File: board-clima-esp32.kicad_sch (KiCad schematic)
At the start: 32 parts, among them IC1 ESP32-S3-WROOM-1-N4, J1 Conn_01x02_Pin, J2 Screw_Terminal_01x03, J3 Conn_01x04_Pin, J4 Conn_01x04_Pin, J5 Conn_01x04_Pin, J6 USB_C_Receptacle, Q1 AO3400A, SW1 RESET, SW2 BOOT, U1 AMS1117-3.3, U2 JZC-32F/C

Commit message: cleanup and some helper in schematic
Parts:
- J4: footprint Connector_PinHeader_1.00mm:PinHeader_1x05_P1.00mm_Vertical -> Connector_PinHeader_2.54mm:PinHeader_1x05_P2.54mm_Vertical
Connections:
- net GND: no longer J6.S1 (SHIELD)
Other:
- note added: "I2C Bus Address: 0x77"
- moved on the sheet: C1, C2, C3, C4, D3, F1, J6, R1, R2, R4, R5, R6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

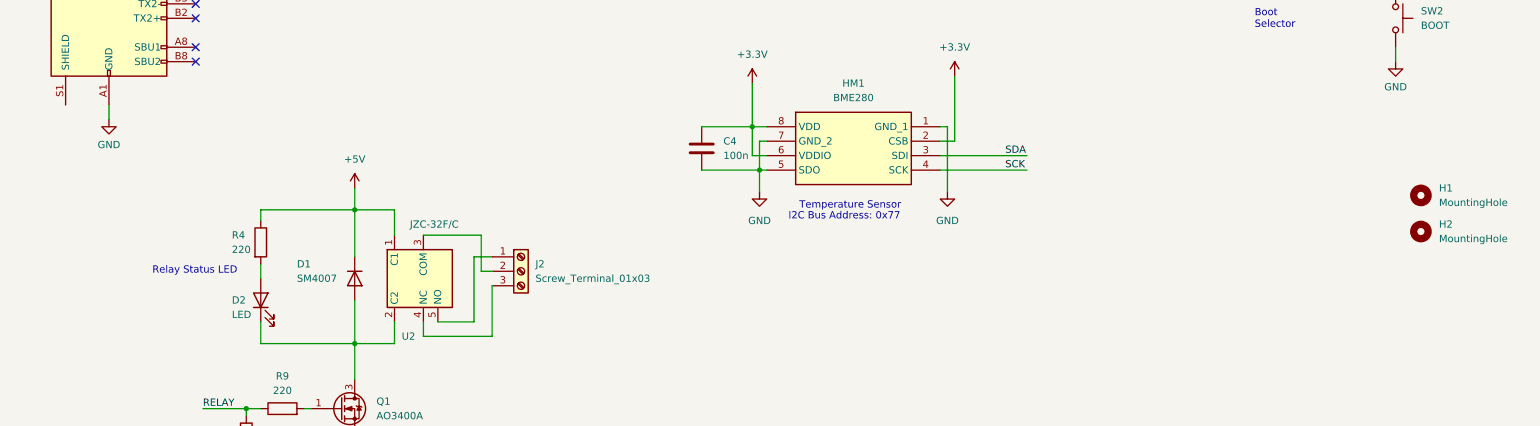
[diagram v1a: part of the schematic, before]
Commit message: added bypass jumper
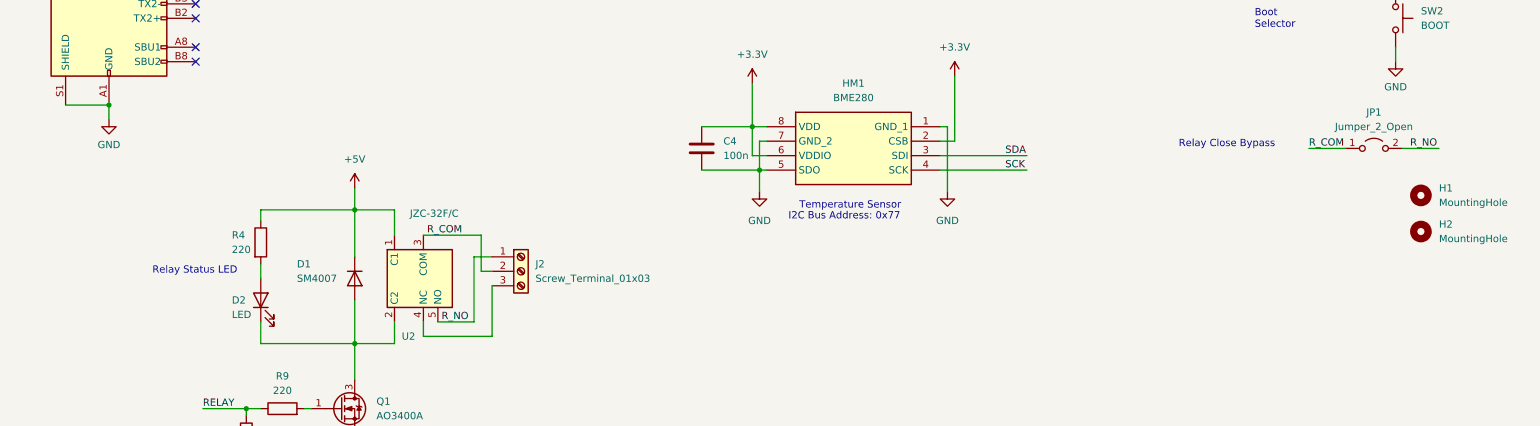
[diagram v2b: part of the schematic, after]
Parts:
- added JP1: Jumper_2_Open, TestPoint:TestPoint_2Pads_Pitch2.54mm_Drill0.8mm, symbol Jumper:Jumper_2_Open
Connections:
- net GND: now also J6.S1 (SHIELD)
- net R_NO: now reaches J2.1 (Pin_1), U2.5 (NO)
- net R_NO: now also JP1.2 (B)
- net R_COM: now reaches J2.2 (Pin_2), U2.3 (COM)
- net R_COM: now also JP1.1 (A)
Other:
- note added: "Relay Close Bypass"
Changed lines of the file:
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@@
     (company "Edoardo Fullin")
+  )
+  (junction (at 30.48 121.92) (diameter 0) (color 0 0 0 0)
   )
   (junction (at 143.51 125.73) (diameter 0) (color 0 0 0 0)
@@
     (stroke (width 0) (type default))
   )
+  (wire (pts (xy 257.81 129.54) (xy 264.16 129.54))
+    (stroke (width 0) (type default))
+  )
   (wire (pts (xy 110.49 74.93) (xy 120.65 74.93))
     (stroke (width 0) (type default))
@@
     (stroke (width 0) (type default))
   )
+  (wire (pts (xy 241.3 129.54) (xy 247.65 129.54))
+    (stroke (width 0) (type default))
+  )
   (wire (pts (xy 97.79 162.56) (xy 85.725 162.56))
     (stroke (width 0) (type default))
   )
   (wire (pts (xy 176.53 82.55) (xy 176.53 85.09))
+    (stroke (width 0) (type default))
+  )
+  (wire (pts (xy 22.86 121.92) (xy 30.48 121.92))
     (stroke (width 0) (type default))
   )
@@
     (effects (font (size 1.27 1.27)) (justify left bottom))
   )
+  (text "Relay Close Bypass" (at 218.44 129.54 0)
+    (effects (font (size 1.27 1.27)) (justify left bottom))
+  )
   (text "Additional\nGPIO" (at 228.6 90.17 0)
     (effects (font (size 1.27 1.27)) (justify left bottom))
@@
     (effects (font (size 1.27 1.27)) (justify left bottom))
   )
+  (label "R_COM" (at 241.3 129.54 0) (fields_autoplaced)
+    (effects (font (size 1.27 1.27)) (justify left bottom))
+  )
+  (label "R_NO" (at 88.9 160.02 0) (fields_autoplaced)
+    (effects (font (size 1.27 1.27)) (justify left bottom))
+  )
   (label "UART_TX" (at 241.3 40.64 0) (fields_autoplaced)
     (effects (font (size 1.27 1.27)) (justify left bottom))
@@
     (effects (font (size 1.27 1.27)) (justify left bottom))
   )
+  (label "R_NO" (at 259.08 129.54 0) (fields_autoplaced)
+    (effects (font (size 1.27 1.27)) (justify left bottom))
+  )
   (label "SDA" (at 241.3 20.32 0) (fields_autoplaced)
     (effects (font (size 1.27 1.27)) (justify left bottom))
@@
   )
   (label "BOOT" (at 182.88 31.75 0) (fields_autoplaced)
+    (effects (font (size 1.27 1.27)) (justify left bottom))
+  )
+  (label "R_COM" (at 86.36 144.78 0) (fields_autoplaced)
     (effects (font (size 1.27 1.27)) (justify left bottom))
   )
@@
         (path "/ec184202-d4fa-4f1f-9fe7-c32d14dd4c20"
           (reference "#PWR07") (unit 1)
+        )
+      )
+    )
+  )
+  (symbol (lib_id "Jumper:Jumper_2_Open") (at 252.73 129.54 0) (unit 1)
+    (in_bom yes) (on_board yes) (dnp no) (fields_autoplaced)
+    (property "Reference" "JP1" (at 252.73 123.19 0)
+      (effects (font (size 1.27 1.27)))
+    )
+    (property "Value" "Jumper_2_Open" (at 252.73 125.73 0)
+      (effects (font (size 1.27 1.27)))
+    )
+    (property "Footprint" "TestPoint:TestPoint_2Pads_Pitch2.54mm_Drill0.8mm" (at 252.73 129.54 0)
+      (effects (font (size 1.27 1.27)) hide)
+    )
+    (property "Datasheet" "~" (at 252.73 129.54 0)
+      (effects (font (size 1.27 1.27)) hide)
+    )
+    (pin "1")
+    (pin "2")
+    (instances
+      (project "board-clima-esp32"
+        (path "/ec184202-d4fa-4f1f-9fe7-c32d14dd4c20"
+          (reference "JP1") (unit 1)
         )
       )
@@
       (effects (font (size 1.27 1.27)) (justify left))
     )
-    (property "Value" "JZC-32F/C" (at 87.63 142.875 0)
-      (effects (font (size 1.27 1.27)))
-    )
+    (property "Value" "JZC-32F/C" (at 87.63 140.97 0)
+      (effects (font (size 1.27 1.27)))
+    )

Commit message: refactor schematic
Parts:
- added R10: 0, symbol Device:R
- J1: symbol Connector:Conn_01x03_Pin -> Connector:Conn_01x04_Pin
- R4, R5: value 220 -> 1k
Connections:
- net +3.3V: now also J1.4 (Pin_4)
- net +5V: now also R10.1; no longer U2.1 (C1)
- net R_NC: now reaches J2.3 (Pin_3), U2.4 (NC)
- new net: R10.2, U2.1 (C1)
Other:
- note added: "Actuators Connections"
- note added: "ESP32S3"
- note added: "External I/O"
- note added: "I2C"
- note added: "JTAG / IO"
- note added: "Junk"
- note added: "Onboard Relay"
- note added: "Onboard Temperature Sensor BME280"
- note added: "Relay ON"
- note added: "Relay Terminals"
- note added: "Relay current limit resistor"
- note added: "USB"
- note removed: "Additional I2C"
- note removed: "JTAG"
- note removed: "Relay Status LED"
- moved on the sheet: C1, C2, C3, C4, D1, D2, D3, F1, H1, H2, HM1, IC1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

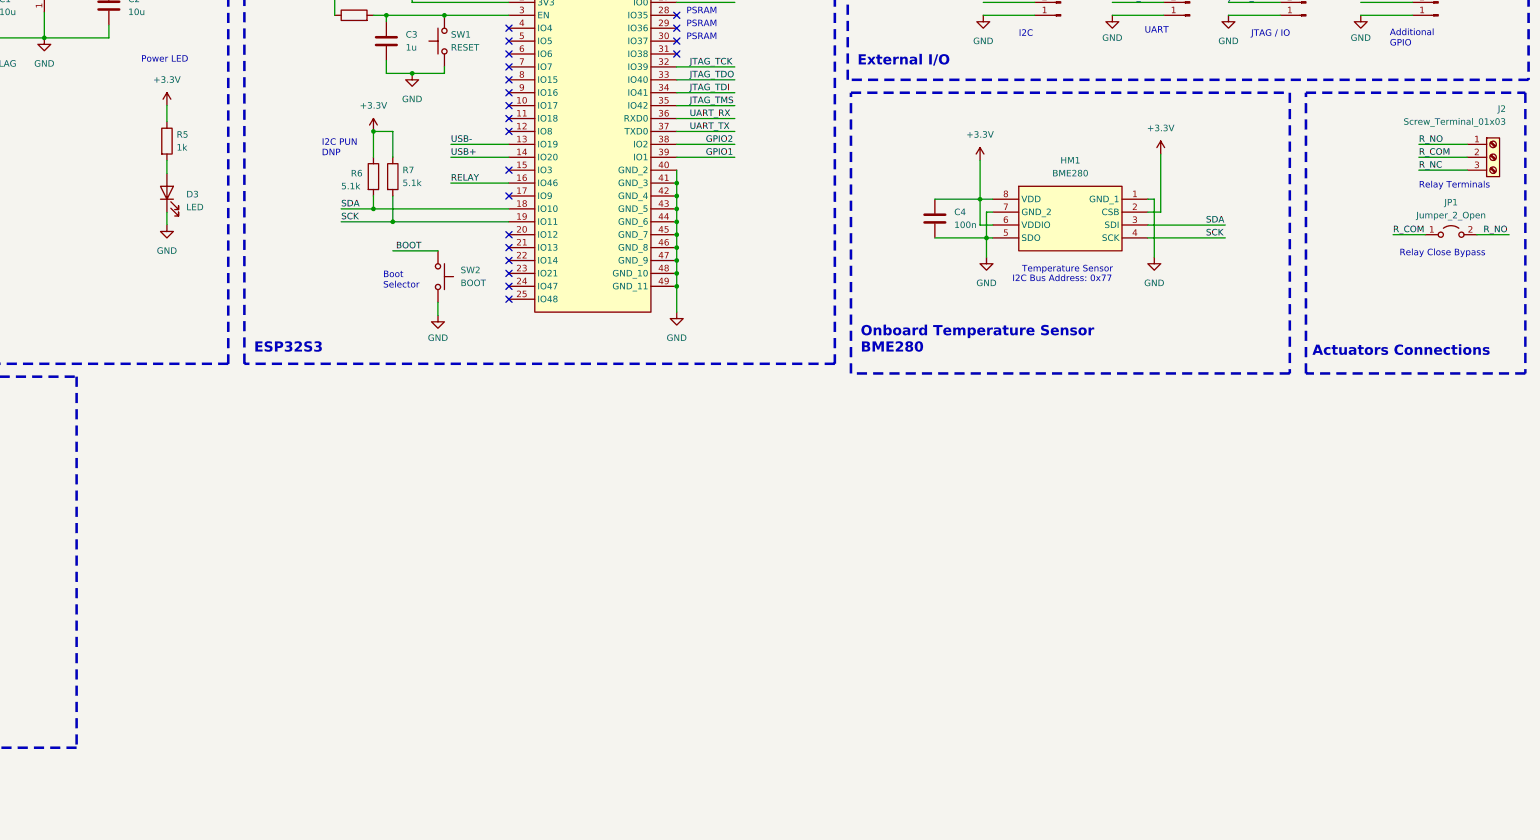
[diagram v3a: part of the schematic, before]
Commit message: OT schematic, relay spice
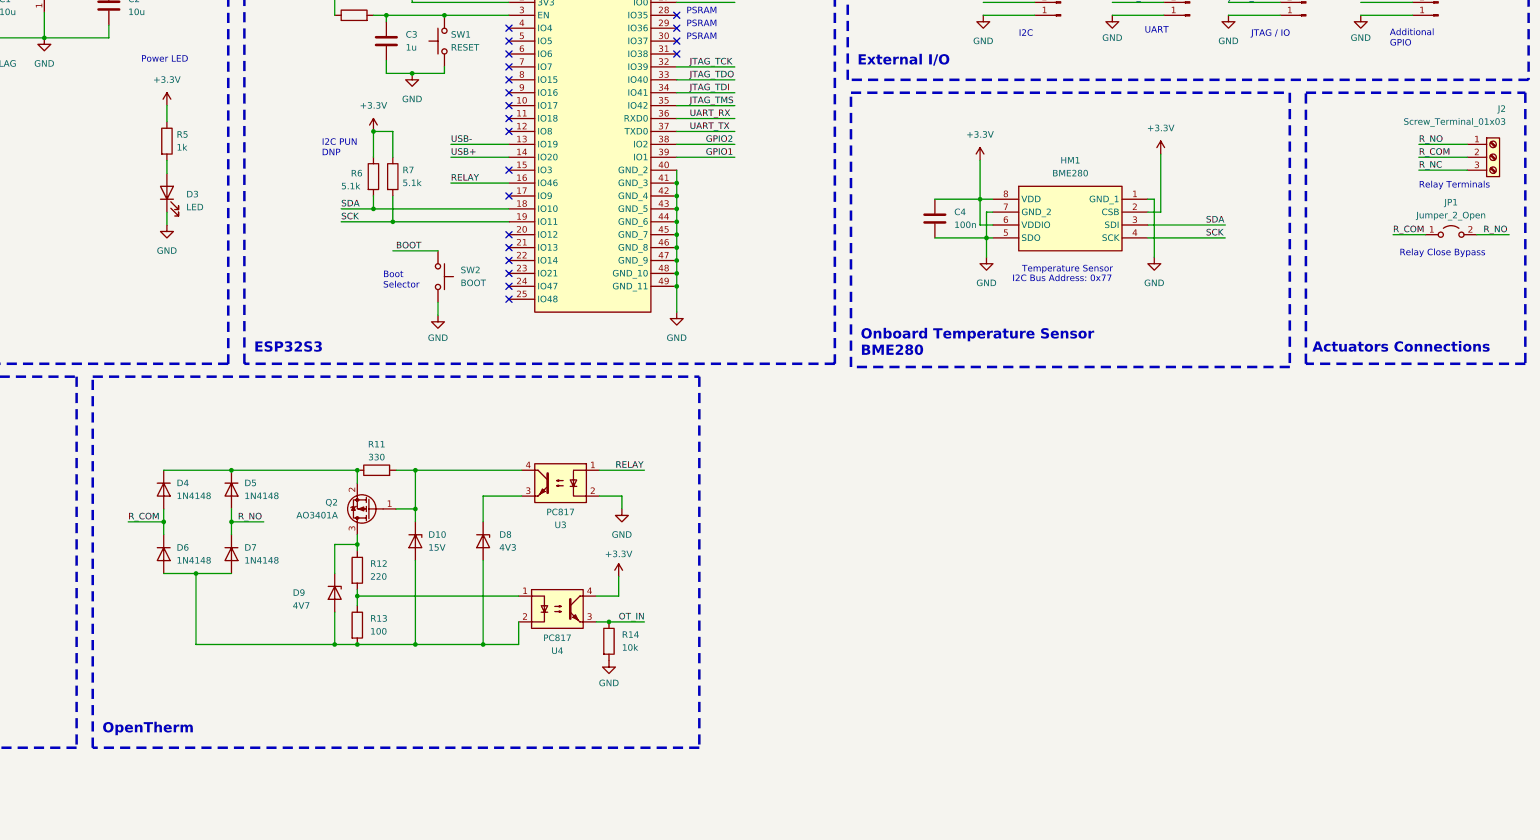
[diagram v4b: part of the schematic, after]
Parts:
- added D10: 15V, symbol Device:D_Zener
- added D4, D5, D6, D7: 1N4148, Diode_THT:D_DO-35_SOD27_P7.62mm_Horizontal, symbol Diode:1N4148
- added D8: 4V3, symbol Device:D_Zener
- added D9: 4V7, symbol Device:D_Zener
- added Q2: AO3401A, Package_TO_SOT_SMD:SOT-23, symbol Transistor_FET:AO3401A
- added R11: 330, symbol Device:R
- added R12: 220, symbol Device:R
- added R13: 100, symbol Device:R
- added R14: 10k, symbol Device:R
- added U3, U4: PC817, Package_DIP:DIP-4_W7.62mm, symbol Isolator:PC817
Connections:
- net +3.3V: now also U4.4
- net GND: now also R14.2, U3.2
- net RELAY: now also U3.1
- net R_COM: now also D4.2 (A), D6.1 (K)
- net R_NO: now also D5.2 (A), D7.1 (K)
- new net: D8.1 (K), U3.3
- new net: D10.2 (A), D6.2 (A), D7.2 (A), D8.2 (A), D9.2 (A), R13.2, U4.2
- new net: R12.2, R13.1, U4.1
- new net: D10.1 (K), Q2.1 (G), R11.2, U3.4
- new net: D9.1 (K), Q2.3 (D), R12.1
- new net: D4.1 (K), D5.1 (K), Q2.2 (S), R11.1
- new net OT_IN: R14.1, U4.3
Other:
- note added: "OpenTherm"

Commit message: rev2 schematic
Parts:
- removed D1: SM4007, Diode_SMD:D_MELF, symbol Diode:SM4007
- removed D2: LED, LED_SMD:LED_0805_2012Metric, symbol Device:LED
- removed J4: Conn_01x04_Pin, Connector_PinHeader_2.54mm:PinHeader_1x05_P2.54mm_Vertical, symbol Connector:Conn_01x05_Pin
- removed U2: JZC-32F/C, JZC-32FC:JZC-32FC, symbol JZC-32F:JZC-32F/C
- added D1, D2: SM4007PL, Diode_THT:D_DO-35_SOD27_P7.62mm_Horizontal, symbol Device:D
- added H3, H4: MountingHole, MountingHole:MountingHole_2.5mm, symbol Mechanical:MountingHole
- added Q3: AO3400A, Package_TO_SOT_SMD:SOT-23, symbol Transistor_FET:AO3400A
- added R15: 330, Resistor_SMD:R_0805_2012Metric, symbol Device:R
- added R16: 220, Resistor_SMD:R_0805_2012Metric, symbol Device:R
- added R17: 10k, Resistor_SMD:R_0805_2012Metric, symbol Device:R
- added U2: ~, HFD2:HFD2-00X-M-L2, symbol HFD2:HFD2/00X-M-L2
- D10, D8, D9: footprint (none) -> Diode_SMD:D_SOD-323
- D4, D5, D6, D7: value 1N4148 -> SM4007PL
- J1: value Conn_01x02_Pin -> Conn_01x06_Pin; symbol Connector:Conn_01x04_Pin -> Connector:Conn_01x06_Pin
- J5: value Conn_01x04_Pin -> Conn_01x05_Pin; symbol Connector:Conn_01x04_Pin -> Connector:Conn_01x05_Pin
- Q1: LCSC C15127 -> (none); Manufacturer_Part_Number AO3401A -> (none)
- R10: value 0 -> 10k; footprint (none) -> Resistor_SMD:R_0805_2012Metric
- R11, R12, R13, R14: footprint (none) -> Resistor_SMD:R_0805_2012Metric
- R4: value 1k -> 0; LCSC C17557 -> (none); Manufacturer_Part_Number 0805W8F2200T5E -> (none)
- R8: value 10k -> 0; LCSC C17414 -> (none); Manufacturer_Part_Number 0805W8F1002T5E -> (none)
- R9: LCSC C17557 -> (none); Manufacturer_Part_Number 0805W8F2200T5E -> (none)
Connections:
- net OT_IN is gone; now on net BOILER_2: R14.1, U4.3
- net +3.3V: now also J1.6 (Pin_6), J5.5 (Pin_5), R4.1, R8.1; no longer J1.4 (Pin_4), J5.4 (Pin_4)
- net +5V: no longer R10.1, R4.1
- net GND: now also J1.5 (Pin_5), J5.4 (Pin_4), R10.1, Q3.2 (S), R17.1; no longer J1.1 (Pin_1), J5.1 (Pin_1), R8.2
- net GPIO1: now also IC1.38 (IO2); no longer IC1.39 (IO1)
- net GPIO2: now also IC1.39 (IO1); no longer IC1.38 (IO2)
- net R_COM: now also U2.4 (CM1)
- net R_NC: now also U2.6 (NC1)
- net R_NO: now also U2.8 (NO1)
- net SCK: now also J1.4 (Pin_4); no longer J1.2 (Pin_2)
- net at R4.2: now also D1.1 (K), U2.16 (S2)
- net GPIO4: now reaches IC1.20 (IO12)
- net GPIO4: now also J1.2 (Pin_2)
- net GPIO5: now reaches IC1.21 (IO13)
- net GPIO5: now also J1.1 (Pin_1)
- net BOILER_1: now reaches IC1.23 (IO21)
- net BOILER_1: now also R15.2, R16.2, R17.2
- net BOILER_2: now reaches IC1.24 (IO47)
- net BOILER_2: now also R10.2, R9.1
- net GPIO3: now reaches IC1.31 (IO38)
- net GPIO3: now also J5.1 (Pin_1)
- net at Q1.3 (D): now also D1.2 (A), U2.1 (S1)
- net at Q1.1 (G): now also R16.1; no longer R9.2
- net JTAG_TCK: no longer names the net of IC1.32 (IO39)
- net JTAG_TDI: no longer names the net of IC1.34 (IO41)
- net JTAG_TDO: no longer names the net of IC1.33 (IO40)
- net JTAG_TMS: no longer names the net of IC1.35 (IO42)
- removed net RELAY: IC1.16 (IO46), R8.1, R9.1, U3.1
- new net: D2.1 (K), R8.2, U2.15 (R2)
- new net: D2.2 (A), Q3.3 (D), U2.2 (R1)
- new net: Q3.1 (G), R9.2
- new net: R15.1, U3.1
- no-connect marks 32 -> 35
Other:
- note added: "I2C Bus Address: 0x76"
- note removed: "I2C"
- note removed: "I2C Bus Address: 0x77"
- note removed: "JTAG / IO"
- note removed: "Relay ON"
- note removed: "Relay current limit resistor"
- moved on the sheet: C1, C2, C3, C4, D10, D3, D4, D5, D6, D7, D8, D9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

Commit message: pcb rev2 placement
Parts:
- added C5: 1u, Capacitor_SMD:C_0805_2012Metric, symbol Device:C
- D1, D2, D4, D5, D6, D7: footprint Diode_THT:D_DO-35_SOD27_P7.62mm_Horizontal -> Diode_SMD:D_SOD-123F
- J1: footprint Connector_PinHeader_2.54mm:PinHeader_1x03_P2.54mm_Vertical -> Connector_PinHeader_2.54mm:PinHeader_1x06_P2.54mm_Vertical
- J5: footprint Connector_PinHeader_2.54mm:PinHeader_1x04_P2.54mm_Vertical -> Connector_PinHeader_2.54mm:PinHeader_1x05_P2.54mm_Vertical
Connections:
- net +3.3V: now also C5.1; no longer R4.1, R8.1
- net +5V: now also R4.1, R8.1
- net BOILER_1: now also IC1.18 (IO10); no longer IC1.23 (IO21)
- net BOILER_2: now also IC1.19 (IO11); no longer IC1.24 (IO47)
- net GND: now also C5.2
- net GPIO4: now also IC1.21 (IO13); no longer IC1.20 (IO12)
- net GPIO5: now also IC1.22 (IO14); no longer IC1.21 (IO13)
- net SCK: now also IC1.24 (IO47), R6.2; no longer IC1.19 (IO11), R7.2
- net SDA: now also IC1.23 (IO21), R7.2; no longer IC1.18 (IO10), R6.2
- net OT_COM: now reaches D10.2 (A), D6.2 (A), D7.2 (A), D8.2 (A), D9.2 (A), R13.2, U4.2
- net OT_HIGH: now reaches D4.1 (K), D5.1 (K), Q2.2 (S), R11.1
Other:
- moved on the sheet: R6, R7
